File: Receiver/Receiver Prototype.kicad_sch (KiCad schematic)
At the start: 14 parts, among them J1 Conn_01x02_Socket, J2 Conn_01x03, J3 Conn_01x02, U1 OPA3692ID

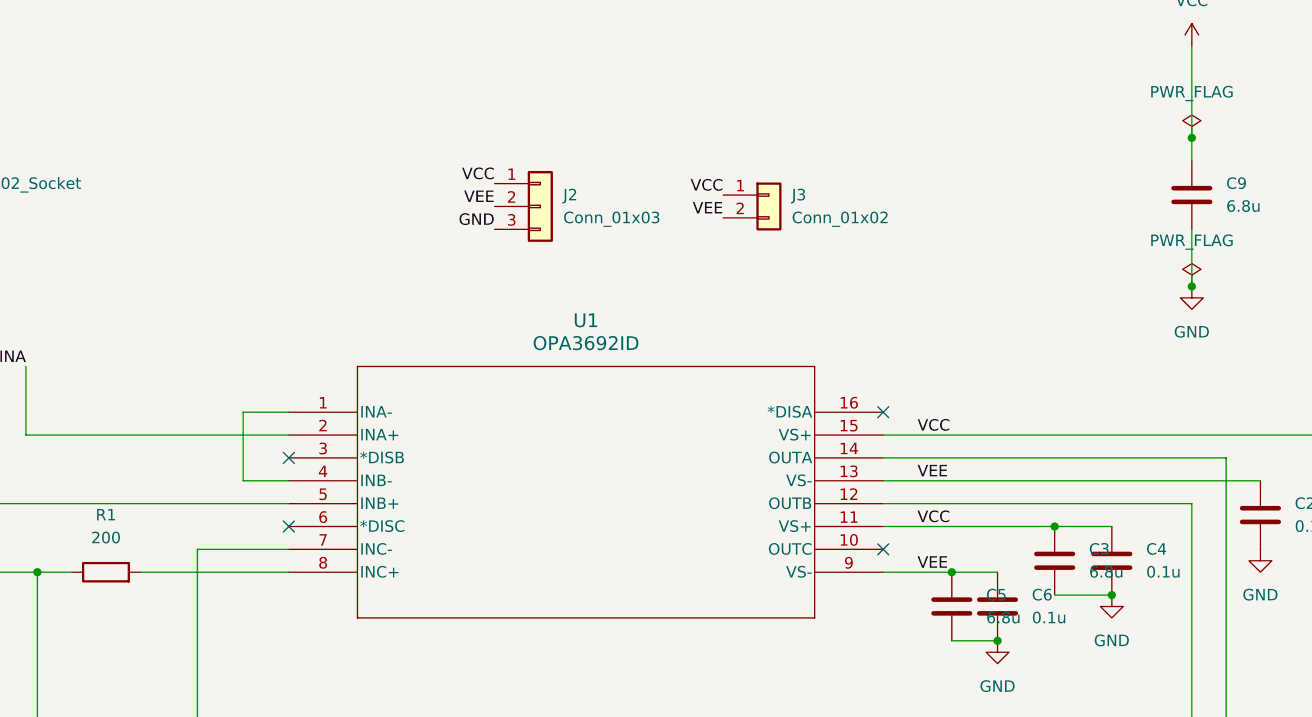
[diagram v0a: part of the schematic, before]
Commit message: added output to schematic at receiver
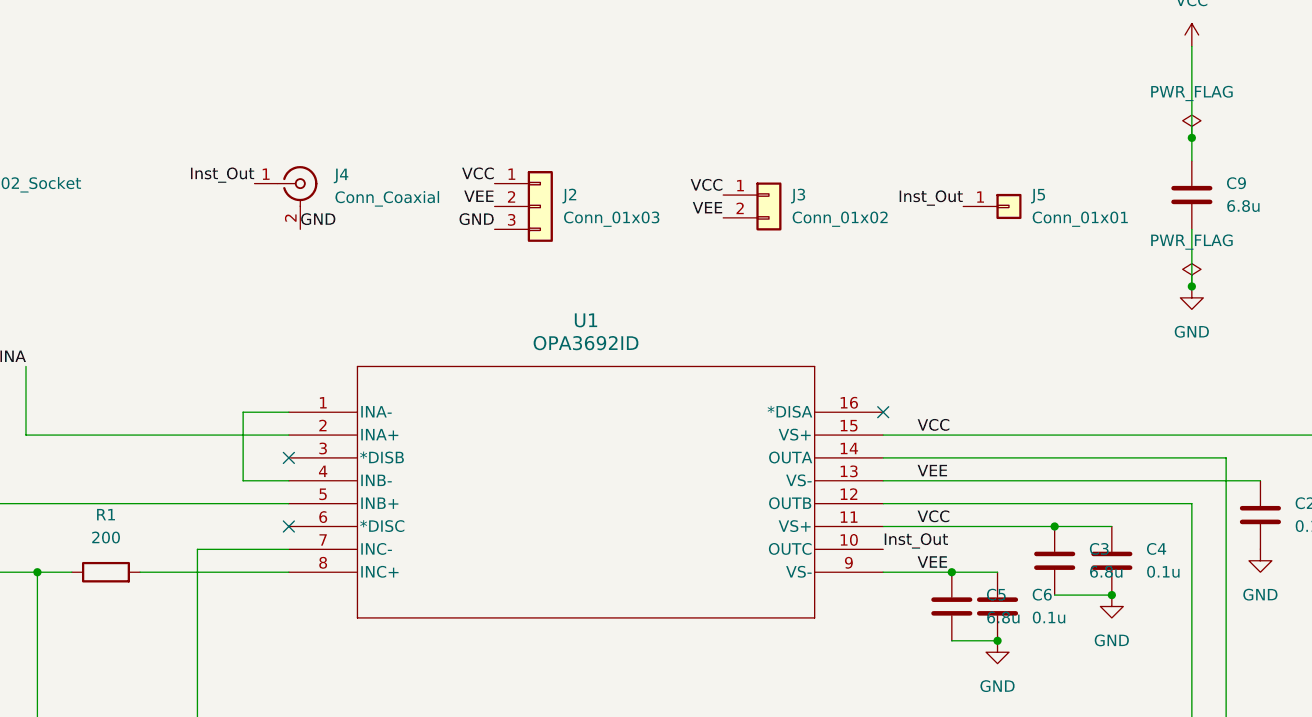
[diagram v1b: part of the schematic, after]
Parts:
- added J4: Conn_Coaxial, symbol Connector:Conn_Coaxial
- added J5: Conn_01x01, symbol Connector_Generic:Conn_01x01
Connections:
- net GND: now also J4.2 (Ext)
- net Inst_Out: now reaches U1.10 (OUTC)
- net Inst_Out: now also J4.1 (In), J5.1 (Pin_1)
- no-connect marks 4 -> 3
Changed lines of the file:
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@@
-	)
-	(no_connect
-		(at 140.97 91.44)
 	)
 	(no_connect
@@
 		)
 	)
-	(label "VCC"
-		(at 144.78 88.9 0)
+	(label "GND"
+		(at 76.2 55.88 0)
 		(fields_autoplaced yes)
 		(effects
@@
 		)
 	)
-	(label "VEE"
-		(at 144.78 83.82 0)
+	(label "VCC"
+		(at 144.78 88.9 0)
 		(fields_autoplaced yes)
 		(effects
@@
 		)
 	)
-	(label "VCC"
-		(at 144.78 78.74 0)
+	(label "VEE"
+		(at 144.78 83.82 0)
 		(fields_autoplaced yes)
 		(effects
@@
 		)
 	)
-	(label "INB"
-		(at 27.94 50.8 180)
+	(label "VCC"
+		(at 144.78 78.74 0)
 		(fields_autoplaced yes)
 		(effects
@@
 				(size 1.27 1.27)
 			)
-			(justify right bottom)
-		)
-	)
-	(label "VEE"
-		(at 97.79 53.34 180)
+			(justify left bottom)
+		)
+	)
+	(label "Inst_Out"
+		(at 149.86 53.34 180)
 		(fields_autoplaced yes)
 		(effects
@@
 		)
 	)
-	(label "VCC"
-		(at 97.79 50.8 180)
+	(label "INB"
+		(at 27.94 50.8 180)
 		(fields_autoplaced yes)
 		(effects
@@
 		)
 	)
-	(label "VEE"
-		(at 144.78 93.98 0)
+	(label "Inst_Out"
+		(at 71.12 50.8 180)
 		(fields_autoplaced yes)
 		(effects
@@
 				(size 1.27 1.27)
 			)
-			(justify left bottom)
-		)
-	)
-	(label "INA"
-		(at 27.94 48.26 180)
+			(justify right bottom)
+		)
+	)
+	(label "VEE"
+		(at 97.79 53.34 180)
 		(fields_autoplaced yes)
 		(effects
@@
 		)
 	)
+	(label "Inst_Out"
+		(at 140.97 91.44 0)
+		(fields_autoplaced yes)
+		(effects
+			(font
+				(size 1.27 1.27)
+			)
+			(justify left bottom)
+		)
+	)
+	(label "VCC"
+		(at 97.79 50.8 180)
+		(fields_autoplaced yes)
+		(effects
+			(font
+				(size 1.27 1.27)
+			)
+			(justify right bottom)
+		)
+	)
+	(label "VEE"
+		(at 144.78 93.98 0)
+		(fields_autoplaced yes)
+		(effects
+			(font
+				(size 1.27 1.27)
+			)
+			(justify left bottom)
+		)
+	)
+	(label "INA"
+		(at 27.94 48.26 180)
+		(fields_autoplaced yes)
+		(effects
+			(font
+				(size 1.27 1.27)
+			)
+			(justify right bottom)
+		)
+	)
 	(symbol
 		(lib_id "power:GND")
@@
 	)
 	(symbol
+		(lib_id "Connector:Conn_Coaxial")
+		(at 76.2 50.8 0)
+		(unit 1)
+		(exclude_from_sim no)
+		(in_bom yes)
+		(on_board yes)
+		(dnp no)
+		(fields_autoplaced yes)
+		(property "Reference" "J4"
+			(at 80.01 49.8231 0)
+			(effects
+				(font
+					(size 1.27 1.27)
+				)
+				(justify left)
+			)
+		)
+		(property "Value" "Conn_Coaxial"
+			(at 80.01 52.3631 0)
+			(effects
+				(font
+					(size 1.27 1.27)
+				)
+				(justify left)
+			)
+		)
+		(property "Footprint" ""
+			(at 76.2 50.8 0)
+			(effects
+				(font
+					(size 1.27 1.27)
+				)
+				(hide yes)
+			)
+		)
+		(property "Datasheet" " ~"
+			(at 76.2 50.8 0)
+			(effects
+				(font
+					(size 1.27 1.27)
+				)
+				(hide yes)
+			)
+		)
+		(property "Description" "coaxial connector (BNC, SMA, SMB, SMC, Cinch/RCA, LEMO, ...)"
+			(at 76.2 50.8 0)
+			(effects
+				(font
+					(size 1.27 1.27)
+				)
+				(hide yes)
+			)
+		)
+		(pin "2"
+		)
+		(pin "1"
+		)
+		(instances
+			(project "Receiver Prototype"
+				(path "/3aa39536-321e-46e0-967e-be2d644a910c"
+					(reference "J4")
+					(unit 1)
+				)
+			)
+		)
+	)
+	(symbol
 		(lib_id "Connector_Generic:Conn_01x02")
 		(at 128.27 52.07 0)
@@
 					(unit 1)
 				)
+			)
+		)
+	)
+	(symbol
+		(lib_id "Connector_Generic:Conn_01x01")
+		(at 154.94 53.34 0)
+		(unit 1)
+		(exclude_from_sim no)
+		(in_bom yes)
+		(on_board yes)
+		(dnp no)
+		(fields_autoplaced yes)
+		(property "Reference" "J5"
+			(at 157.48 52.0699 0)
+			(effects
+				(font
+					(size 1.27 1.27)
+				)
+				(justify left)
+			)
+		)
+		(property "Value" "Conn_01x01"
+			(at 157.48 54.6099 0)
+			(effects
+				(font
+					(size 1.27 1.27)
+				)
+				(justify left)
+			)
+		)
+		(property "Footprint" ""
+			(at 154.94 53.34 0)
+			(effects
+				(font
+					(size 1.27 1.27)
+				)
+				(hide yes)
+			)
+		)
+		(property "Datasheet" "~"
+			(at 154.94 53.34 0)
+			(effects
+				(font
+					(size 1.27 1.27)
+				)
+				(hide yes)
+			)
+		)
+		(property "Description" "Generic connector, single row, 01x01, script generated (kicad-library-utils/schlib/autogen/connector/)"
+			(at 154.94 53.34 0)
+			(effects
+				(font
+					(size 1.27 1.27)
+				)
+				(hide yes)
+			)
+		)
+		(pin "1"
+		)
+		(instances
+			(project "Receiver Prototype"
+				(path "/3aa39536-321e-46e0-967e-be2d644a910c"
+					(reference "J5")
+					(unit 1)
+				)

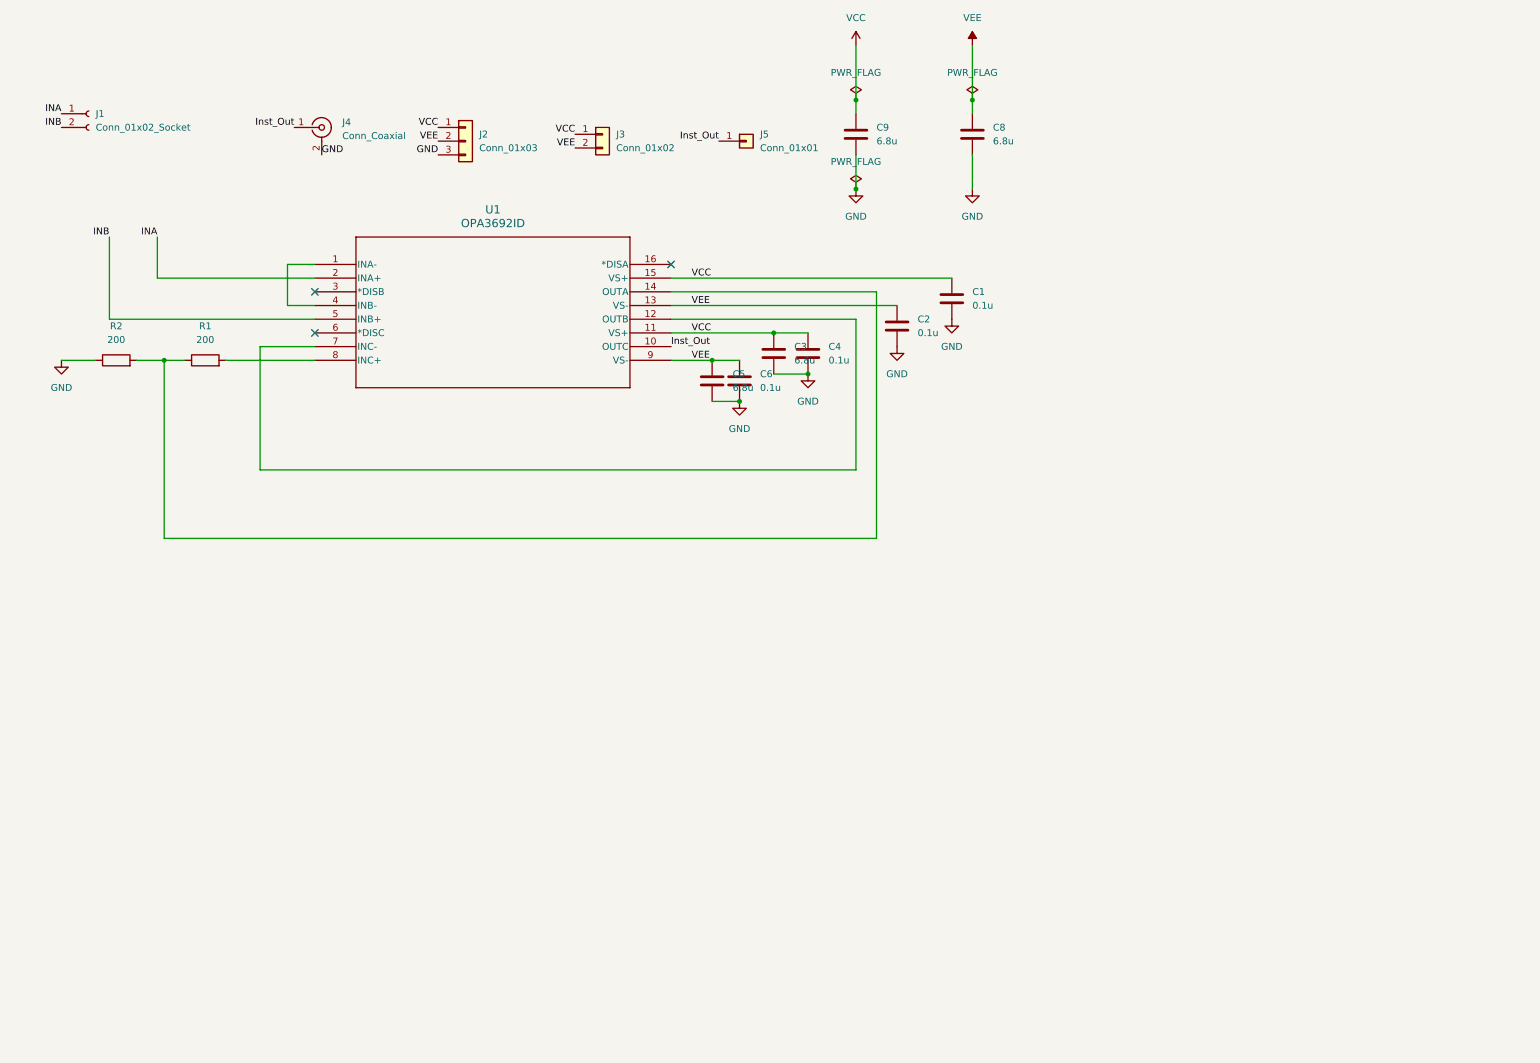
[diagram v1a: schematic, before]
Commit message: Finished receiver prototype schematic
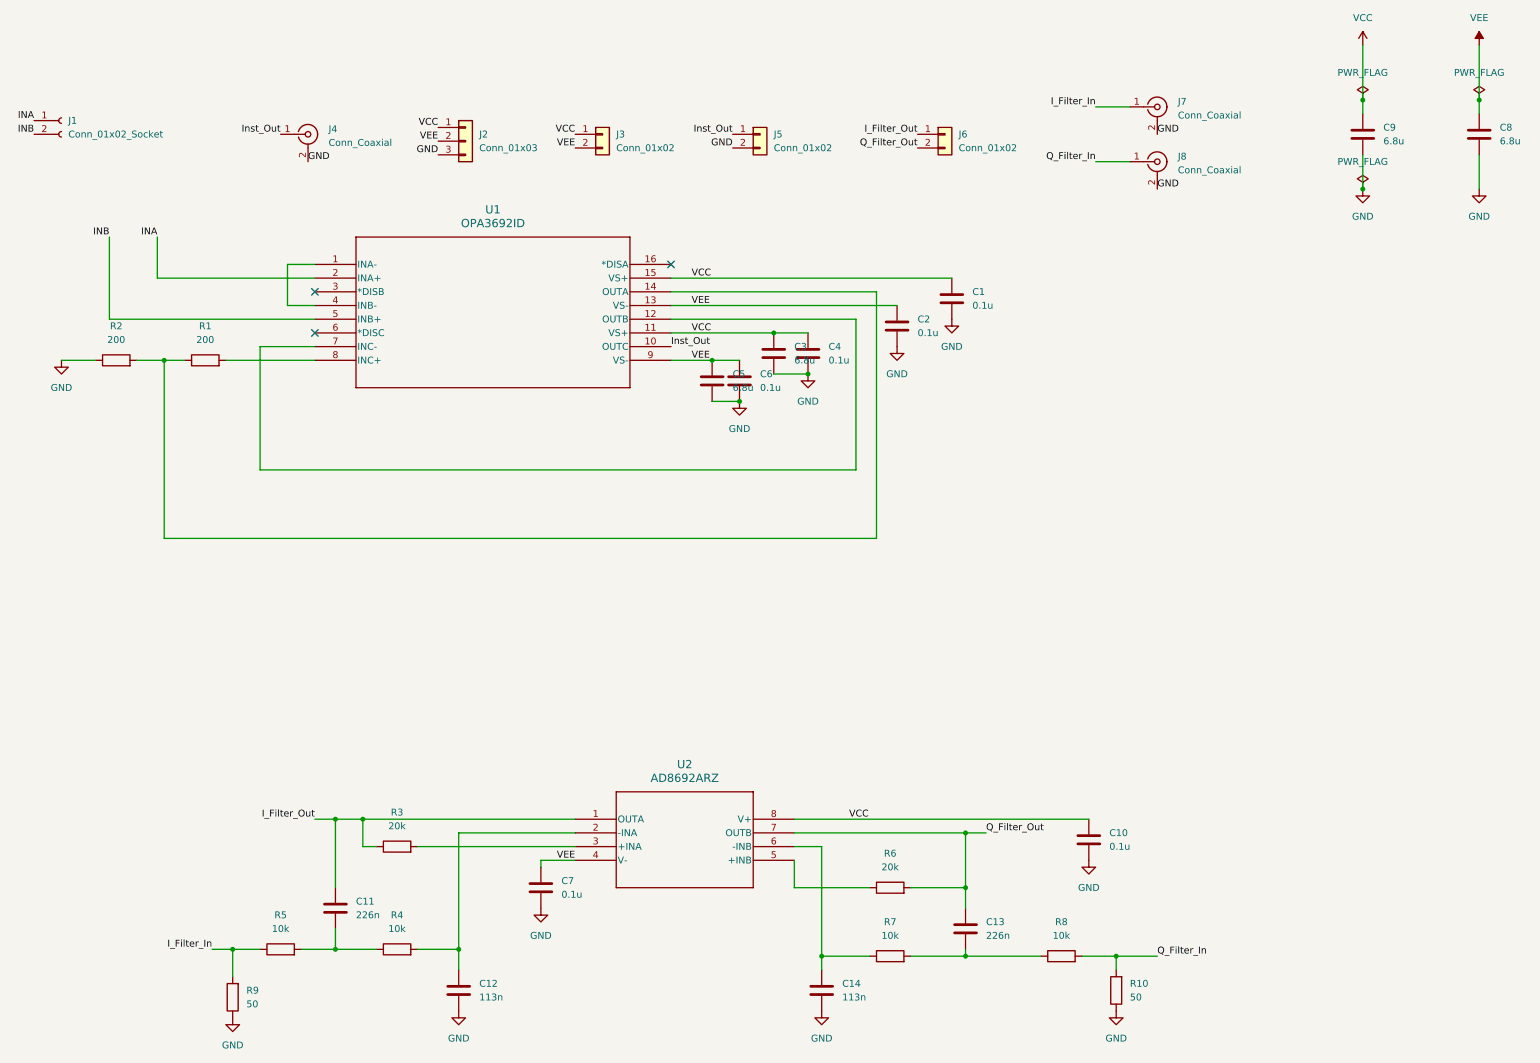
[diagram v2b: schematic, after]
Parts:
- removed J5: Conn_01x01, symbol Connector_Generic:Conn_01x01
- added C10, C7: 0.1u, symbol Device:C
- added C11, C13: 226n, symbol Device:C
- added C12, C14: 113n, symbol Device:C
- added J5, J6: Conn_01x02, symbol Connector_Generic:Conn_01x02
- added J7, J8: Conn_Coaxial, symbol Connector:Conn_Coaxial
- added R10, R9: 50, symbol Device:R
- added R3, R6: 20k, symbol Device:R
- added R4, R5, R7, R8: 10k, symbol Device:R
- added U2: AD8692ARZ, R-8_ADI, symbol AD8692:AD8692ARZ
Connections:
- net GND: now also C10.2, C12.2, C14.2, C7.2, J5.2 (Pin_2), J7.2 (Ext), J8.2 (Ext), R10.1, R9.1
- net Inst_Out: now also J5.1 (Pin_1)
- net VCC: now also C10.1, U2.8 (V+)
- net VEE: now also C7.1, U2.4 (V-)
- new net: C14.1, R7.1, U2.6 (-INB)
- new net: R6.1, U2.5 (+INB)
- new net: C11.2, R4.1, R5.2
- new net: R3.2, U2.3 (+INA)
- new net: C12.1, R4.2, U2.2 (-INA)
- new net: C13.2, R7.2, R8.1
- new net I_Filter_In: J7.1 (In), R5.1, R9.2
- new net I_Filter_Out: C11.1, J6.1 (Pin_1), R3.1, U2.1 (OUTA)
- new net Q_Filter_In: J8.1 (In), R10.2, R8.2
- new net Q_Filter_Out: C13.1, J6.2 (Pin_2), R6.2, U2.7 (OUTB)
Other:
- moved on the sheet: C8, C9, J1, J4

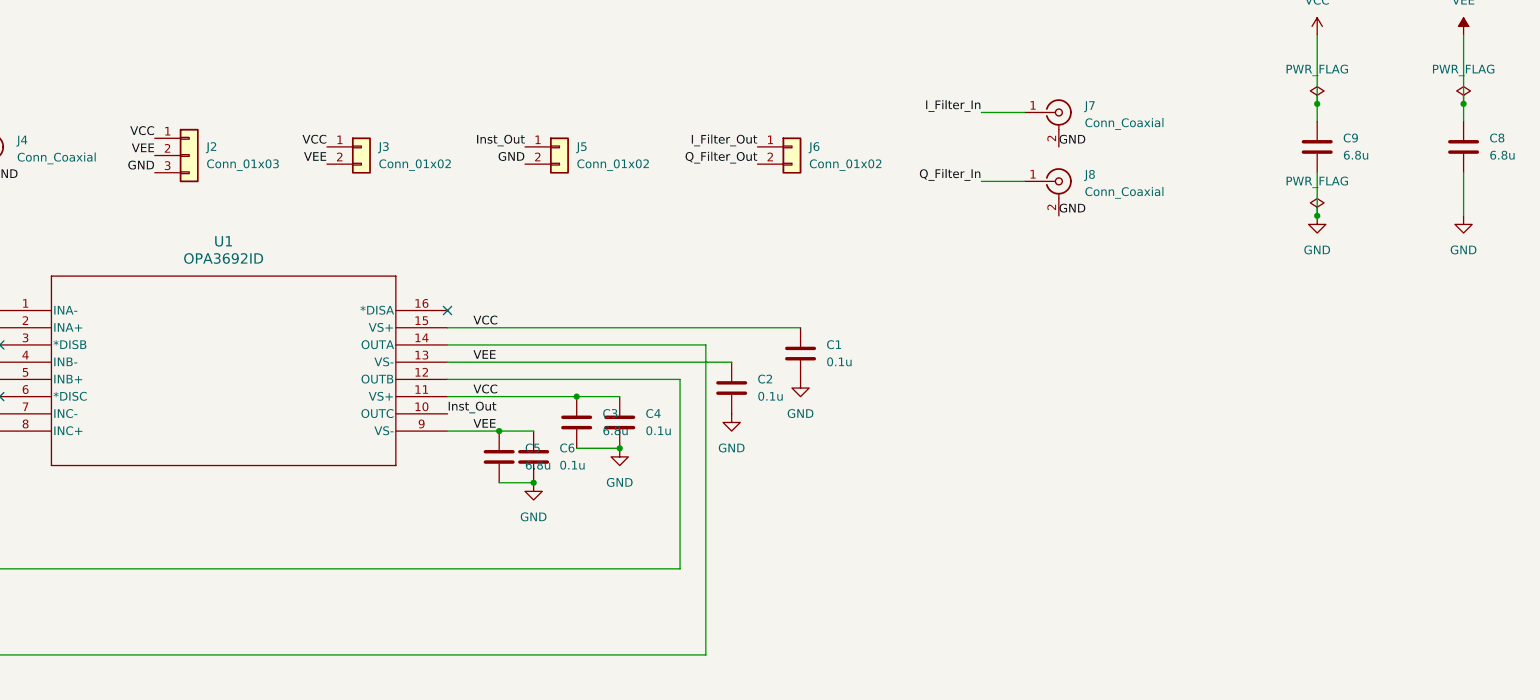
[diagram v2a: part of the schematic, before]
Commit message: First receiver pcb layout (not connected)
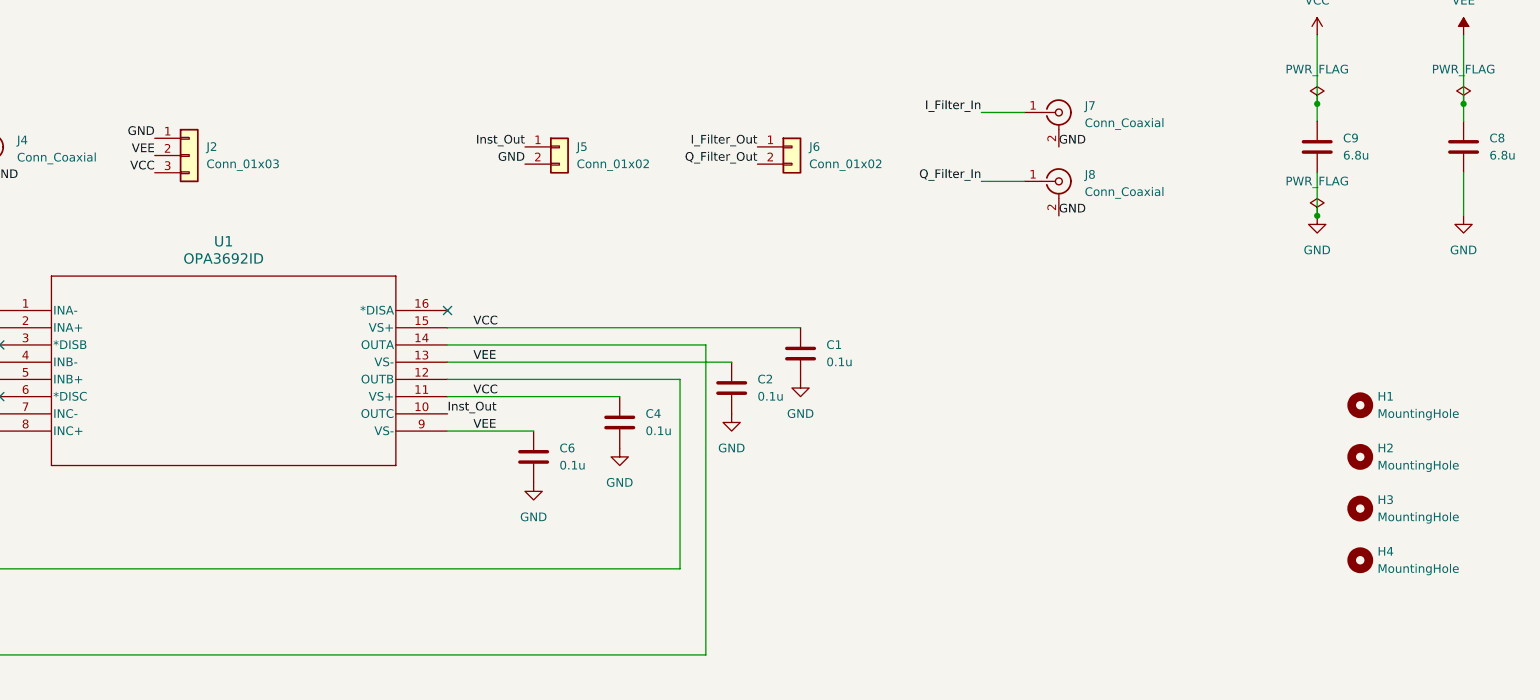
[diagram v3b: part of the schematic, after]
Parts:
- removed C3, C5: 6.8u, symbol Device:C
- removed J3: Conn_01x02, symbol Connector_Generic:Conn_01x02
- added H1, H2, H3, H4: MountingHole, MountingHole:MountingHole_2.5mm_Pad, symbol Mechanical:MountingHole
- C1, C10, C11, C12, C13, C14, C2, C4, C6, C7: footprint (none) -> Capacitor_SMD:C_0805_2012Metric_Pad1.18x1.45mm_HandSolder
- J1: footprint (none) -> Connector_PinSocket_2.54mm:PinSocket_1x02_P2.54mm_Vertical
- J2: footprint (none) -> Connector_PinHeader_2.54mm:PinHeader_1x03_P2.54mm_Vertical
- J4, J7, J8: footprint (none) -> Connector_Coaxial:SMA_Amphenol_132134_Vertical
- J5, J6: footprint (none) -> Connector_PinHeader_2.54mm:PinHeader_1x02_P2.54mm_Vertical
- R1, R10, R2, R3, R4, R5, R6, R7, R8, R9: footprint (none) -> Resistor_SMD:R_0805_2012Metric_Pad1.20x1.40mm_HandSolder
- U2: footprint R-8_ADI -> AD8692:R-8_ADI
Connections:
- net GND: now also J2.1 (Pin_1); no longer J2.3 (Pin_3)
- net VCC: now also J2.3 (Pin_3); no longer J2.1 (Pin_1)
